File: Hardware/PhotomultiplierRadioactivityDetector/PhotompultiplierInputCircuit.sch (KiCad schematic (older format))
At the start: 29 parts

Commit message: placement of components for tube driver
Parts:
- C19: footprint Capacitor_THT:C_Disc_D11.0mm_W5.0mm_P7.50mm -> Capacitor_SMD:C_1210_3225Metric
- C20, C21, C22, C23, C24, C26, C27, C28, C29, C33, C34: footprint Capacitor_SMD:C_1206_3216Metric -> Capacitor_SMD:C_1210_3225Metric
- R32, R33, R34: footprint Resistor_THT:R_Axial_DIN0411_L9.9mm_D3.6mm_P12.70mm_Horizontal -> Resistor_SMD:R_MELF_MMB-0207
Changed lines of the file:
@@
 F 0 "C26" H 3235 1446 50  0000 R CNN
 F 1 "10n/3kV" H 3235 1355 50  0000 R CNN
-F 2 "Capacitor_SMD:C_1206_3216Metric" H 3388 1250 50  0001 C CNN
+F 2 "Capacitor_SMD:C_1210_3225Metric" H 3388 1250 50  0001 C CNN
 F 3 "~" H 3350 1400 50  0001 C CNN
 	1    3350 1400
@@
 F 0 "C27" H 3235 2496 50  0000 R CNN
 F 1 "10n/3kV" H 3235 2405 50  0000 R CNN
-F 2 "Capacitor_SMD:C_1206_3216Metric" H 3388 2300 50  0001 C CNN
+F 2 "Capacitor_SMD:C_1210_3225Metric" H 3388 2300 50  0001 C CNN
 F 3 "~" H 3350 2450 50  0001 C CNN
 	1    3350 2450
@@
 F 0 "C28" H 3235 3646 50  0000 R CNN
 F 1 "10n/3kV" H 3235 3555 50  0000 R CNN
-F 2 "Capacitor_SMD:C_1206_3216Metric" H 3388 3450 50  0001 C CNN
+F 2 "Capacitor_SMD:C_1210_3225Metric" H 3388 3450 50  0001 C CNN
 F 3 "~" H 3350 3600 50  0001 C CNN
 	1    3350 3600
@@
 F 0 "C29" H 3235 4746 50  0000 R CNN
 F 1 "10n/3kV" H 3235 4655 50  0000 R CNN
-F 2 "Capacitor_SMD:C_1206_3216Metric" H 3388 4550 50  0001 C CNN
+F 2 "Capacitor_SMD:C_1210_3225Metric" H 3388 4550 50  0001 C CNN
 F 3 "~" H 3350 4700 50  0001 C CNN
 	1    3350 4700
@@
 F 0 "C33" H 3235 5796 50  0000 R CNN
 F 1 "10n/3kV" H 3235 5705 50  0000 R CNN
-F 2 "Capacitor_SMD:C_1206_3216Metric" H 3388 5600 50  0001 C CNN
+F 2 "Capacitor_SMD:C_1210_3225Metric" H 3388 5600 50  0001 C CNN
 F 3 "~" H 3350 5750 50  0001 C CNN
 	1    3350 5750
@@
 F 0 "C34" H 3235 6846 50  0000 R CNN
 F 1 "10n/3kV" H 3235 6755 50  0000 R CNN
-F 2 "Capacitor_SMD:C_1206_3216Metric" H 3388 6650 50  0001 C CNN
+F 2 "Capacitor_SMD:C_1210_3225Metric" H 3388 6650 50  0001 C CNN
 F 3 "~" H 3350 6800 50  0001 C CNN
 	1    3350 6800
@@
 F 0 "C19" V 1748 6600 50  0000 C CNN
 F 1 "10n/3kV" V 1839 6600 50  0000 C CNN
-F 2 "Capacitor_THT:C_Disc_D11.0mm_W5.0mm_P7.50mm" H 2038 6450 50  0001 C CNN
+F 2 "Capacitor_SMD:C_1210_3225Metric" H 2038 6450 50  0001 C CNN
 F 3 "~" H 2000 6600 50  0001 C CNN
 	1    2000 6600
@@
 F 0 "R32" H 1720 6946 50  0000 L CNN
 F 1 "150k" H 1720 6855 50  0000 L CNN
-F 2 "Resistor_THT:R_Axial_DIN0411_L9.9mm_D3.6mm_P12.70mm_Horizontal" V 1580 6900 50  0001 C CNN
+F 2 "Resistor_SMD:R_MELF_MMB-0207" V 1580 6900 50  0001 C CNN
 F 3 "~" H 1650 6900 50  0001 C CNN
 	1    1650 6900
@@
 F 0 "R34" V 2243 6600 50  0000 C CNN
 F 1 "150k" V 2334 6600 50  0000 C CNN
-F 2 "Resistor_THT:R_Axial_DIN0411_L9.9mm_D3.6mm_P12.70mm_Horizontal" V 2380 6600 50  0001 C CNN
+F 2 "Resistor_SMD:R_MELF_MMB-0207" V 2380 6600 50  0001 C CNN
 F 3 "~" H 2450 6600 50  0001 C CNN
 	1    2450 6600
@@
 F 0 "C20" H 3235 1996 50  0000 R CNN
 F 1 "10n/3kV" H 3235 1905 50  0000 R CNN
-F 2 "Capacitor_SMD:C_1206_3216Metric" H 3388 1800 50  0001 C CNN
+F 2 "Capacitor_SMD:C_1210_3225Metric" H 3388 1800 50  0001 C CNN
 F 3 "~" H 3350 1950 50  0001 C CNN
 	1    3350 1950
@@
 F 0 "C21" H 3235 3096 50  0000 R CNN
 F 1 "10n/3kV" H 3235 3005 50  0000 R CNN
-F 2 "Capacitor_SMD:C_1206_3216Metric" H 3388 2900 50  0001 C CNN
+F 2 "Capacitor_SMD:C_1210_3225Metric" H 3388 2900 50  0001 C CNN
 F 3 "~" H 3350 3050 50  0001 C CNN
 	1    3350 3050
@@
 F 0 "C22" H 3235 4196 50  0000 R CNN
 F 1 "10n/3kV" H 3235 4105 50  0000 R CNN
-F 2 "Capacitor_SMD:C_1206_3216Metric" H 3388 4000 50  0001 C CNN
+F 2 "Capacitor_SMD:C_1210_3225Metric" H 3388 4000 50  0001 C CNN
 F 3 "~" H 3350 4150 50  0001 C CNN
 	1    3350 4150
@@
 F 0 "C23" H 3235 5296 50  0000 R CNN
 F 1 "10n/3kV" H 3235 5205 50  0000 R CNN
-F 2 "Capacitor_SMD:C_1206_3216Metric" H 3388 5100 50  0001 C CNN
+F 2 "Capacitor_SMD:C_1210_3225Metric" H 3388 5100 50  0001 C CNN
 F 3 "~" H 3350 5250 50  0001 C CNN
 	1    3350 5250
@@
 F 0 "C24" H 3235 6346 50  0000 R CNN
 F 1 "10n/3kV" H 3235 6255 50  0000 R CNN
-F 2 "Capacitor_SMD:C_1206_3216Metric" H 3388 6150 50  0001 C CNN
+F 2 "Capacitor_SMD:C_1210_3225Metric" H 3388 6150 50  0001 C CNN
 F 3 "~" H 3350 6300 50  0001 C CNN
 	1    3350 6300
@@
 F 0 "R33" V 6143 6750 50  0000 C CNN
 F 1 "150k" V 6234 6750 50  0000 C CNN
-F 2 "Resistor_THT:R_Axial_DIN0411_L9.9mm_D3.6mm_P12.70mm_Horizontal" V 6280 6750 50  0001 C CNN
+F 2 "Resistor_SMD:R_MELF_MMB-0207" V 6280 6750 50  0001 C CNN
 F 3 "~" H 6350 6750 50  0001 C CNN
 	1    6350 6750

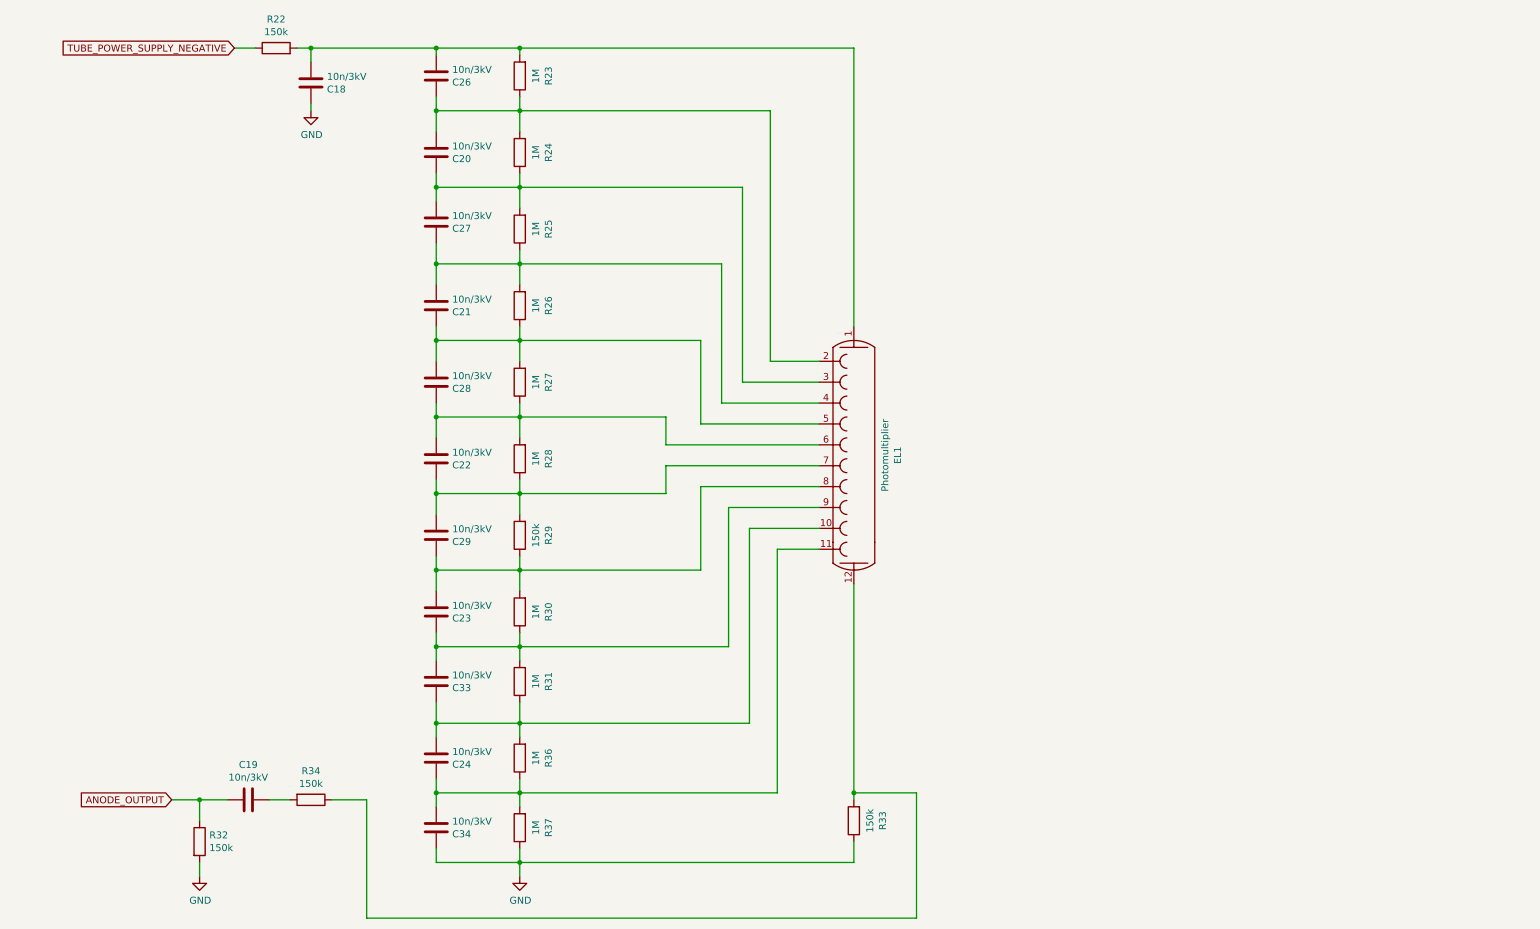
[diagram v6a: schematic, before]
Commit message: split for continous and pulse mode
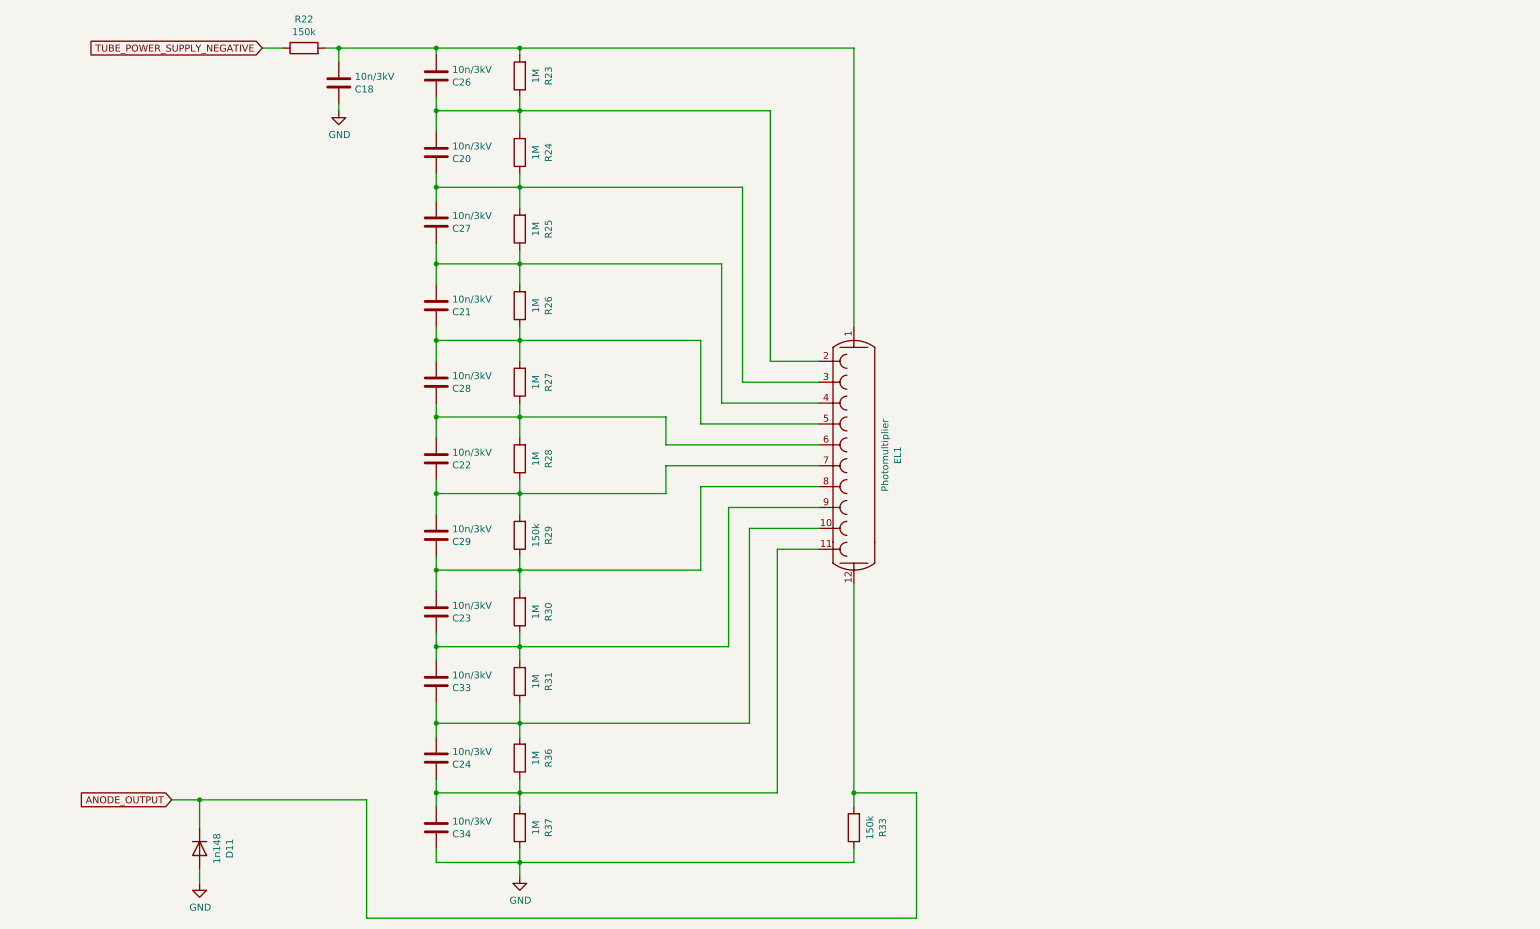
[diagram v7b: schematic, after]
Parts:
- removed C19: 10n/3kV, Capacitor_SMD:C_1210_3225Metric, symbol Device:C
- removed R32, R34: 150k, Resistor_SMD:R_MELF_MMB-0207, symbol Device:R
- added D11: 1n148, Diode_SMD:D_MELF, symbol Device:D
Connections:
- net ANODE_OUTPUT: now also EL1.12, R33.2, D11.1 (K)
- net GND: now also D11.2 (A)
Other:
- moved on the sheet: C18, R22, R33
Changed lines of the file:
@@
 $Descr A4 11693 8268
 encoding utf-8
-Sheet 4 6
+Sheet 4 7
 Title ""
 Date ""
@@
 L Device:R R22
 U 1 1 5ED76D14
-P 2200 1200
-F 0 "R22" V 2407 1200 50  0000 C CNN
-F 1 "150k" V 2316 1200 50  0000 C CNN
-F 2 "Resistor_THT:R_Axial_DIN0411_L9.9mm_D3.6mm_P12.70mm_Horizontal" V 2130 1200 50  0001 C CNN
-F 3 "~" H 2200 1200 50  0001 C CNN
-	1    2200 1200
+P 2400 1200
+F 0 "R22" V 2607 1200 50  0000 C CNN
+F 1 "150k" V 2516 1200 50  0000 C CNN
+F 2 "Resistor_THT:R_Axial_DIN0411_L9.9mm_D3.6mm_P12.70mm_Horizontal" V 2330 1200 50  0001 C CNN
+F 3 "~" H 2400 1200 50  0001 C CNN
+	1    2400 1200
 	0    -1   -1   0
 $EndComp
@@
 L Device:C C18
 U 1 1 5ED772BA
-P 2450 1450
-F 0 "C18" H 2335 1496 50  0000 R CNN
-F 1 "10n/3kV" H 2335 1405 50  0000 R CNN
-F 2 "Capacitor_THT:C_Disc_D11.0mm_W5.0mm_P7.50mm" H 2488 1300 50  0001 C CNN
-F 3 "~" H 2450 1450 50  0001 C CNN
-	1    2450 1450
+P 2650 1450
+F 0 "C18" H 2535 1496 50  0000 R CNN
+F 1 "10n/3kV" H 2535 1405 50  0000 R CNN
+F 2 "Capacitor_THT:C_Disc_D11.0mm_W5.0mm_P7.50mm" H 2688 1300 50  0001 C CNN
+F 3 "~" H 2650 1450 50  0001 C CNN
+	1    2650 1450
 	-1   0    0    1
 $EndComp
@@
 L power:GND #PWR034
 U 1 1 5ED77786
-P 2450 1650
-F 0 "#PWR034" H 2450 1400 50  0001 C CNN
-F 1 "GND" H 2455 1477 50  0000 C CNN
-F 2 "" H 2450 1650 50  0001 C CNN
-F 3 "" H 2450 1650 50  0001 C CNN
-	1    2450 1650
+P 2650 1650
+F 0 "#PWR034" H 2650 1400 50  0001 C CNN
+F 1 "GND" H 2655 1477 50  0000 C CNN
+F 2 "" H 2650 1650 50  0001 C CNN
+F 3 "" H 2650 1650 50  0001 C CNN
+	1    2650 1650
 	1    0    0    -1
 $EndComp
@@
 	3950 1250 3950 1200
 Wire Wire Line
-	2350 1200 2450 1200
+	2550 1200 2650 1200
 Connection ~ 3950 1200
-Text GLabel 1900 1200 0    50   Input ~ 0
+Text GLabel 2100 1200 0    50   Input ~ 0
 TUBE_POWER_SUPPLY_NEGATIVE
 Text GLabel 1450 6600 0    50   Input ~ 0
@@
 	6350 1200 3950 1200
 Wire Wire Line
-	2450 1650 2450 1600
-Wire Wire Line
-	2450 1300 2450 1200
-Connection ~ 2450 1200
+	2650 1650 2650 1600
+Wire Wire Line
+	2650 1300 2650 1200
+Connection ~ 2650 1200
 $Comp
 L Device:C C26
@@
 	3350 7050 3350 6950
 Wire Wire Line
-	2050 1200 1900 1200
-$Comp
-L Device:C C19
-U 1 1 5EEDAF04
-P 2000 6600
-F 0 "C19" V 1748 6600 50  0000 C CNN
-F 1 "10n/3kV" V 1839 6600 50  0000 C CNN
-F 2 "Capacitor_SMD:C_1210_3225Metric" H 2038 6450 50  0001 C CNN
-F 3 "~" H 2000 6600 50  0001 C CNN
-	1    2000 6600
-	0    1    1    0
-$EndComp
-$Comp
-L Device:R R32
-U 1 1 5EEDB740
-P 1650 6900
-F 0 "R32" H 1720 6946 50  0000 L CNN
-F 1 "150k" H 1720 6855 50  0000 L CNN
-F 2 "Resistor_SMD:R_MELF_MMB-0207" V 1580 6900 50  0001 C CNN
-F 3 "~" H 1650 6900 50  0001 C CNN
-	1    1650 6900
-	1    0    0    -1
-$EndComp
-$Comp
-L power:GND #PWR035
-U 1 1 5EEDBFFB
-P 1650 7150
-F 0 "#PWR035" H 1650 6900 50  0001 C CNN
-F 1 "GND" H 1655 6977 50  0000 C CNN
-F 2 "" H 1650 7150 50  0001 C CNN
-F 3 "" H 1650 7150 50  0001 C CNN
-	1    1650 7150
-	1    0    0    -1
-$EndComp
-$Comp
-L Device:R R34
-U 1 1 5EEE2BFA
-P 2450 6600
-F 0 "R34" V 2243 6600 50  0000 C CNN
-F 1 "150k" V 2334 6600 50  0000 C CNN
-F 2 "Resistor_SMD:R_MELF_MMB-0207" V 2380 6600 50  0001 C CNN
-F 3 "~" H 2450 6600 50  0001 C CNN
-	1    2450 6600
-	0    1    1    0
-$EndComp
-Wire Wire Line
-	2300 6600 2150 6600
-Wire Wire Line
-	1650 7150 1650 7050
-Wire Wire Line
-	1850 6600 1650 6600
-Wire Wire Line
-	1650 6750 1650 6600
+	2250 1200 2100 1200
 Connection ~ 1650 6600
 Wire Wire Line
@@
 L Device:R R33
 U 1 1 5EE29B31
-P 6350 6750
-F 0 "R33" V 6143 6750 50  0000 C CNN
-F 1 "150k" V 6234 6750 50  0000 C CNN
-F 2 "Resistor_SMD:R_MELF_MMB-0207" V 6280 6750 50  0001 C CNN
-F 3 "~" H 6350 6750 50  0001 C CNN
-	1    6350 6750
-	-1   0    0    1
-$EndComp
-Wire Wire Line
-	6350 6600 6350 6550
-Wire Wire Line
-	6350 6900 6350 7050
-Wire Wire Line
-	2450 1200 3350 1200
+P 6350 6800
+F 0 "R33" V 6143 6800 50  0000 C CNN
+F 1 "150k" V 6234 6800 50  0000 C CNN
+F 2 "Resistor_SMD:R_MELF_MMB-0207" V 6280 6800 50  0001 C CNN
+F 3 "~" H 6350 6800 50  0001 C CNN
+	1    6350 6800
+	-1   0    0    1
+$EndComp
+Wire Wire Line
+	6350 6650 6350 6550
+Wire Wire Line
+	6350 6950 6350 7050
+Wire Wire Line
+	2650 1200 3350 1200
 Wire Wire Line
 	6350 6550 6800 6550
@@
 Wire Wire Line
 	6350 6550 6350 5050
-Wire Wire Line
-	2850 6600 2600 6600
+$Comp
+L Device:D D?
+U 1 1 5EE7139E
+P 1650 6950
+AR Path="/5EDA53F3/5EE7139E" Ref="D?"  Part="1"
+AR Path="/5EFA52FA/5EE7139E" Ref="D?"  Part="1"
+AR Path="/5EDA585D/5EE7139E" Ref="D11"  Part="1"
+F 0 "D11" H 1650 7166 50  0000 C CNN
+F 1 "1n148" H 1650 7075 50  0000 C CNN
+F 2 "Diode_SMD:D_MELF" H 1650 6950 50  0001 C CNN
+F 3 "~" H 1650 6950 50  0001 C CNN
+	1    1650 6950
+	0    1    1    0
+$EndComp
+$Comp
+L power:GND #PWR?
+U 1 1 5EE713AA
+P 1650 7200
+AR Path="/5EF1F288/5EE713AA" Ref="#PWR?"  Part="1"
+AR Path="/5EDA53F3/5EE713AA" Ref="#PWR?"  Part="1"
+AR Path="/5EFA52FA/5EE713AA" Ref="#PWR?"  Part="1"
+AR Path="/5EDA585D/5EE713AA" Ref="#PWR02"  Part="1"
+F 0 "#PWR02" H 1650 6950 50  0001 C CNN
+F 1 "GND" H 1655 7027 50  0000 C CNN
+F 2 "" H 1650 7200 50  0001 C CNN
+F 3 "" H 1650 7200 50  0001 C CNN
+	1    1650 7200
+	1    0    0    -1
+$EndComp
+Wire Wire Line
+	1650 7100 1650 7200
+Wire Wire Line
+	1650 6600 1650 6800
+Wire Wire Line
+	1650 6600 2850 6600
 $EndSCHEMATC

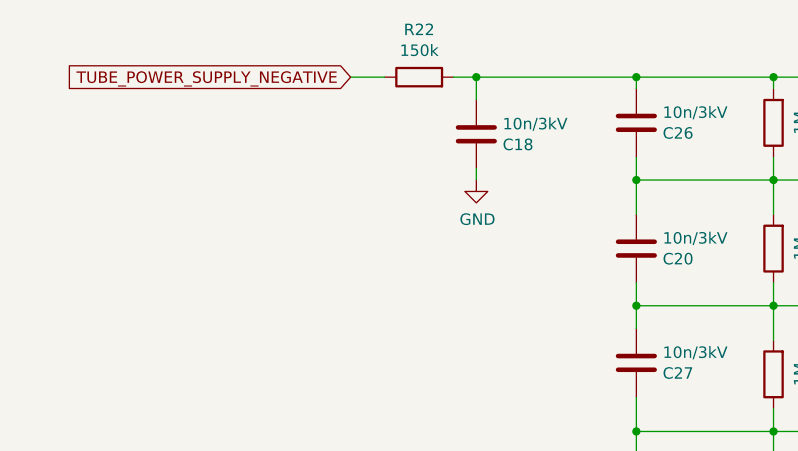
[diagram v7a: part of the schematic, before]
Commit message: fix footprints
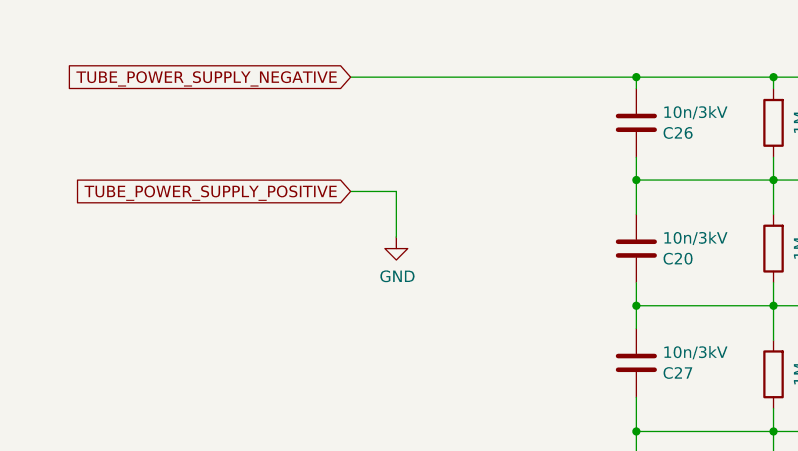
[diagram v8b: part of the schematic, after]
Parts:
- removed C18: 10n/3kV, Capacitor_THT:C_Disc_D11.0mm_W5.0mm_P7.50mm, symbol Device:C
- removed R22: 150k, Resistor_THT:R_Axial_DIN0411_L9.9mm_D3.6mm_P12.70mm_Horizontal, symbol Device:R
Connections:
- net TUBE_POWER_SUPPLY_NEGATIVE: now also C26.2, EL1.1, R23.2
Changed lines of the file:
@@
 	-1   0    0    1
-$EndComp
-$Comp
-L Device:R R22
-U 1 1 5ED76D14
-P 2400 1200
-F 0 "R22" V 2607 1200 50  0000 C CNN
-F 1 "150k" V 2516 1200 50  0000 C CNN
-F 2 "Resistor_THT:R_Axial_DIN0411_L9.9mm_D3.6mm_P12.70mm_Horizontal" V 2330 1200 50  0001 C CNN
-F 3 "~" H 2400 1200 50  0001 C CNN
-	1    2400 1200
-	0    -1   -1   0
-$EndComp
-$Comp
-L Device:C C18
-U 1 1 5ED772BA
-P 2650 1450
-F 0 "C18" H 2535 1496 50  0000 R CNN
-F 1 "10n/3kV" H 2535 1405 50  0000 R CNN
-F 2 "Capacitor_THT:C_Disc_D11.0mm_W5.0mm_P7.50mm" H 2688 1300 50  0001 C CNN
-F 3 "~" H 2650 1450 50  0001 C CNN
-	1    2650 1450
-	-1   0    0    1
-$EndComp
-$Comp
-L power:GND #PWR034
-U 1 1 5ED77786
-P 2650 1650
-F 0 "#PWR034" H 2650 1400 50  0001 C CNN
-F 1 "GND" H 2655 1477 50  0000 C CNN
-F 2 "" H 2650 1650 50  0001 C CNN
-F 3 "" H 2650 1650 50  0001 C CNN
-	1    2650 1650
-	1    0    0    -1
 $EndComp
 Wire Wire Line
 	3950 1250 3950 1200
-Wire Wire Line
-	2550 1200 2650 1200
 Connection ~ 3950 1200
 Text GLabel 2100 1200 0    50   Input ~ 0
@@
 Wire Wire Line
 	6350 1200 3950 1200
-Wire Wire Line
-	2650 1650 2650 1600
-Wire Wire Line
-	2650 1300 2650 1200
-Connection ~ 2650 1200
 $Comp
 L Device:C C26
@@
 Wire Wire Line
 	3350 1250 3350 1200
-Connection ~ 3350 1200
 Wire Wire Line
 	3350 1200 3950 1200
@@
 Wire Wire Line
 	3350 7050 3350 6950
-Wire Wire Line
-	2250 1200 2100 1200
 Connection ~ 1650 6600
 Wire Wire Line
@@
 Wire Wire Line
 	6350 6950 6350 7050
-Wire Wire Line
-	2650 1200 3350 1200
 Wire Wire Line
 	6350 6550 6800 6550
@@
 Wire Wire Line
 	1650 6600 2850 6600
+Wire Wire Line
+	2100 1200 3350 1200
+Connection ~ 3350 1200
+Text GLabel 2100 1700 0    50   Input ~ 0
+TUBE_POWER_SUPPLY_POSITIVE
+$Comp
+L power:GND #PWR013
+U 1 1 5F0BAFBA
+P 2300 1900
+F 0 "#PWR013" H 2300 1650 50  0001 C CNN
+F 1 "GND" H 2305 1727 50  0000 C CNN
+F 2 "" H 2300 1900 50  0001 C CNN
+F 3 "" H 2300 1900 50  0001 C CNN
+	1    2300 1900
+	1    0    0    -1
+$EndComp
+Wire Wire Line
+	2100 1700 2300 1700
+Wire Wire Line
+	2300 1700 2300 1900
 $EndSCHEMATC
